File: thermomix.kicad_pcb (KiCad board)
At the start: 4 copper layers, 61.5 x 33.4 mm, 65 parts, among them J101 DX07S016JA1R1500, J102 Conn_01x05, J201 Conn_02x12_Odd_Even, SW101 SW_Push, SW102 SW_Push, U101 MIC5353-3.3YMT, U102 TPD2E2U06, U103 STM32F303RDTx, U201 LTC2983, Y101 Crystal_GND24

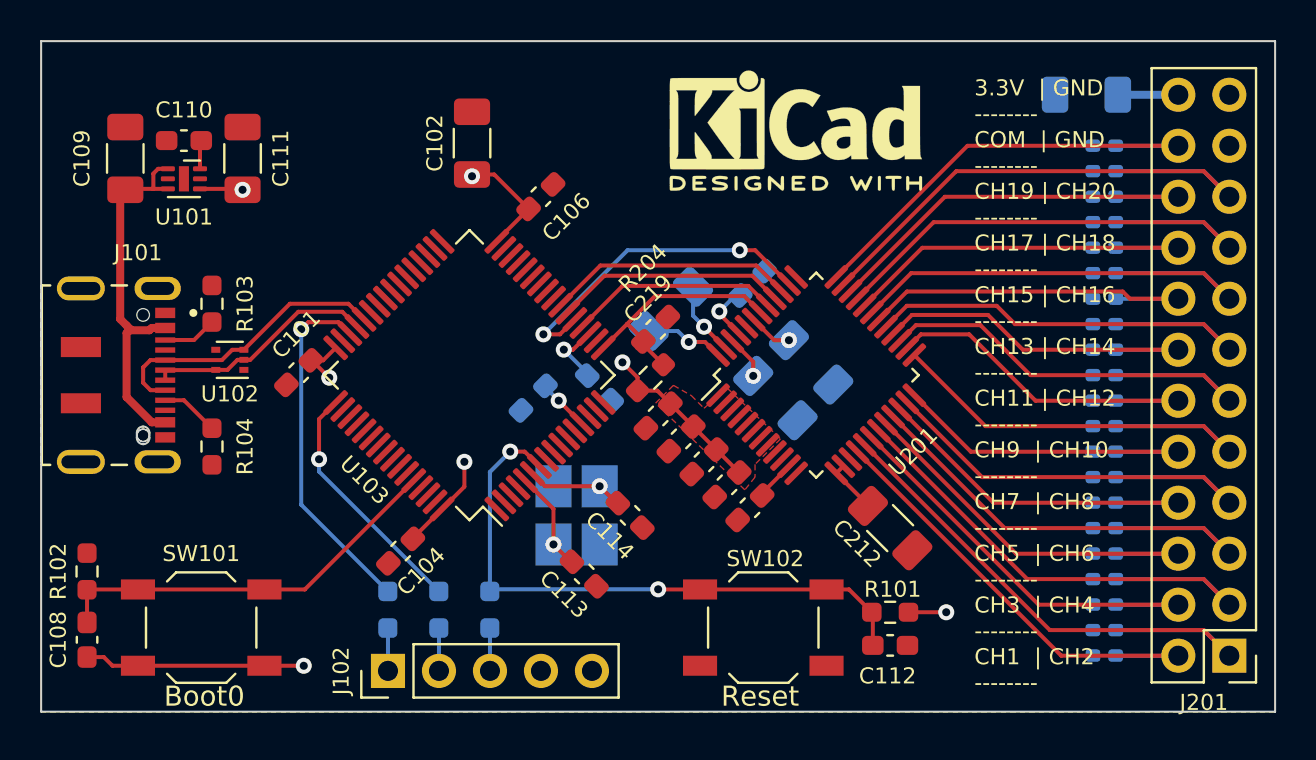
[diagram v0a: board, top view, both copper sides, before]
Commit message: Fixes issues from revision 1.0
Signed-off-by: Alexis Jeandet <alexis.jeandet@member.fsf.org>
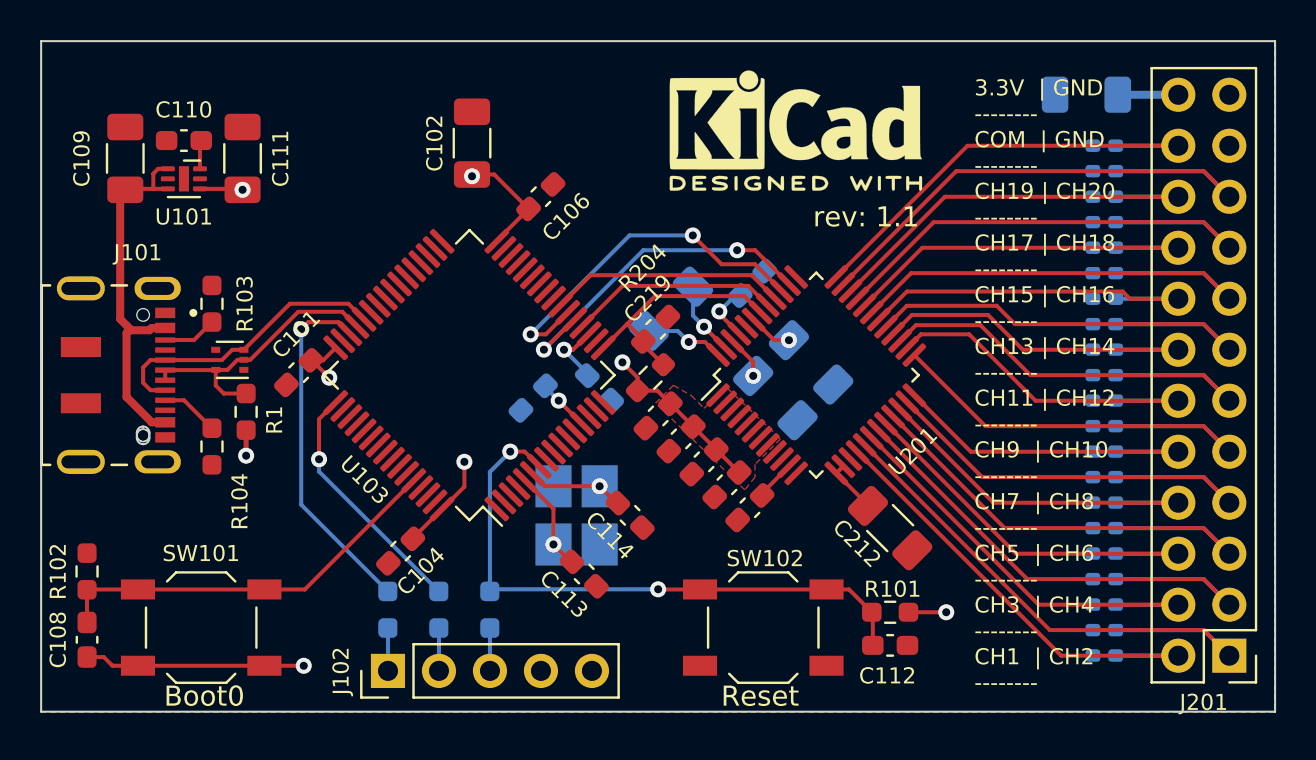
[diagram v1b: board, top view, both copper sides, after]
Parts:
- added R1: 5.1k, Resistor_SMD:R_0603_1608Metric_Pad0.98x0.95mm_HandSolder, F.Cu at (107.2, 92.3)
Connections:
- U102 pad 2: /USB_D+ -> unconnected-(U102-Pad2)
- U103 pad 22: /SPI1_MOSI -> /SPI1_MISO
- U103 pad 23: /SPI1_MISO -> /SPI1_MOSI
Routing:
- net /SPI1_MISO: track 12.4 -> 18.0 mm, vias 0 -> 2
- net /USB_D+: track 11.6 -> 14.0 mm
- net /3.3V: track 49.5 -> 50.7 mm, vias 10 -> 11
- net /SPI1_SCK: track 16.5 -> 17.1 mm
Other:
- board text added: "rev: 1.1"
